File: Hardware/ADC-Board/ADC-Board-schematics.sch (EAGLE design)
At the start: 20 parts

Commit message: layouts
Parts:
- removed CDCS502: CDCS502, components:CDCS502
- removed IC6: (no value), SparkFun-PowerIC:V_REG_TPS76433SOT23-5
- added U$1: CDCS502TSSOP-8, components:CDCS502TSSOP-8
- added U1: (no value), SparkFun-PowerIC:V_REG_LM1117SOT223
- C28: value (none) -> 10uF
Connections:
- net +12VDC: now also U1.IN; no longer IC6.EN, IC6.IN
- net 3V3: now also U$1.VDD; no longer CDCS502.VDD
- net 5VCC: now also U1.OUT, U1.OUT@1; no longer IC6.OUT
- net GND: now also U$1.FS, U$1.GND, U$1.SSC_SEL_0, U$1.SSC_SEL_1, U1.ADJ; no longer CDCS502.FS, CDCS502.GND, CDCS502.SSC_SEL_0, CDCS502.SSC_SEL_1, IC6.GND
- net N$29: now also U$1.XIN; no longer CDCS502.XIN
- net N$30: now also U$1.XOUT; no longer CDCS502.XOUT
- net N$32: now also U$1.CLK_OUT; no longer CDCS502.CLK_OUT
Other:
- moved on the sheet: C28

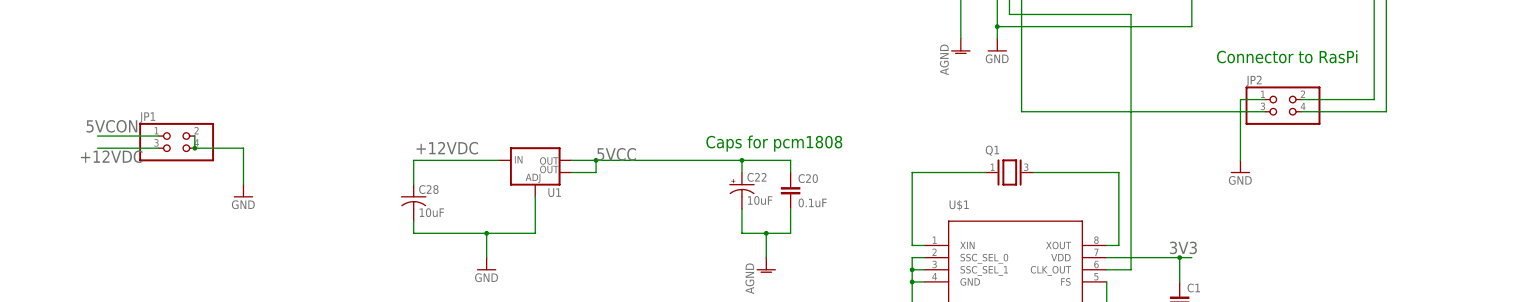
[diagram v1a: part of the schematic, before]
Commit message: tvs considerations
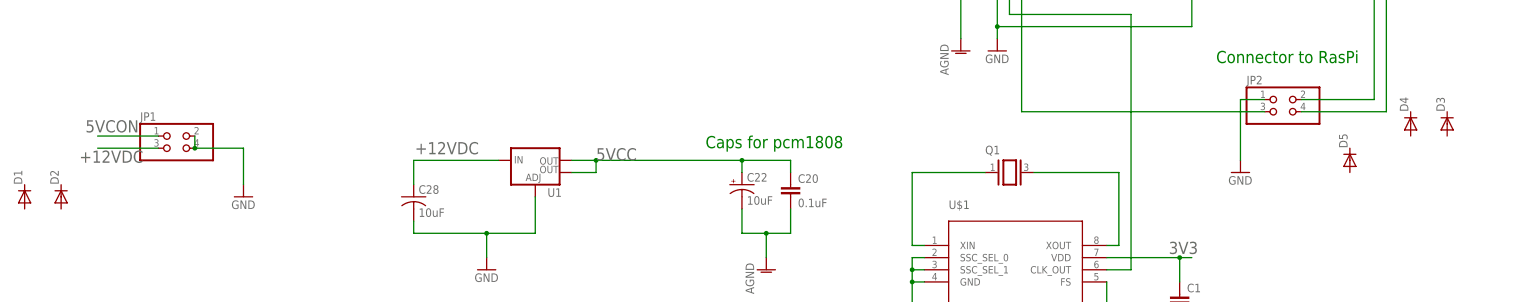
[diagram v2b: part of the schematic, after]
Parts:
- added D1, D2, D3, D4, D5: (no value), diode:DIODE-DO-214AC
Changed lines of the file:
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@@
 <grid distance="0.1" unitdist="inch" unit="inch" style="lines" multiple="1" display="no" altdistance="0.01" altunitdist="inch" altunit="inch"/>
 <layers>
-<layer number="1" name="Top" color="4" fill="1" visible="yes" active="no"/>
-<layer number="2" name="Route2" color="1" fill="3" visible="yes" active="no"/>
-<layer number="3" name="Route3" color="4" fill="3" visible="yes" active="no"/>
-<layer number="4" name="Route4" color="1" fill="4" visible="yes" active="no"/>
-<layer number="5" name="Route5" color="4" fill="4" visible="yes" active="no"/>
-<layer number="6" name="Route6" color="1" fill="8" visible="yes" active="no"/>
-<layer number="7" name="Route7" color="4" fill="8" visible="yes" active="no"/>
-<layer number="8" name="Route8" color="1" fill="2" visible="yes" active="no"/>
-<layer number="9" name="Route9" color="4" fill="2" visible="yes" active="no"/>
-<layer number="10" name="Route10" color="1" fill="7" visible="yes" active="no"/>
-<layer number="11" name="Route11" color="4" fill="7" visible="yes" active="no"/>
-<layer number="12" name="Route12" color="1" fill="5" visible="yes" active="no"/>
-<layer number="13" name="Route13" color="4" fill="5" visible="yes" active="no"/>
-<layer number="14" name="Route14" color="1" fill="6" visible="yes" active="no"/>
-<layer number="15" name="Route15" color="4" fill="6" visible="yes" active="no"/>
-<layer number="16" name="Bottom" color="1" fill="1" visible="yes" active="no"/>
-<layer number="17" name="Pads" color="2" fill="1" visible="yes" active="no"/>
-<layer number="18" name="Vias" color="2" fill="1" visible="yes" active="no"/>
-<layer number="19" name="Unrouted" color="6" fill="1" visible="yes" active="no"/>
-<layer number="20" name="Dimension" color="15" fill="1" visible="yes" active="no"/>
-<layer number="21" name="tPlace" color="7" fill="1" visible="yes" active="no"/>
-<layer number="22" name="bPlace" color="7" fill="1" visible="yes" active="no"/>
-<layer number="23" name="tOrigins" color="15" fill="1" visible="yes" active="no"/>
-<layer number="24" name="bOrigins" color="15" fill="1" visible="yes" active="no"/>
-<layer number="25" name="tNames" color="7" fill="1" visible="yes" active="no"/>
-<layer number="26" name="bNames" color="7" fill="1" visible="yes" active="no"/>
-<layer number="27" name="tValues" color="7" fill="1" visible="yes" active="no"/>
-<layer number="28" name="bValues" color="7" fill="1" visible="yes" active="no"/>
+<layer number="1" name="Top" color="4" fill="1" visible="no" active="no"/>
+<layer number="2" name="Route2" color="1" fill="3" visible="no" active="no"/>
+<layer number="3" name="Route3" color="4" fill="3" visible="no" active="no"/>
+<layer number="4" name="Route4" color="1" fill="4" visible="no" active="no"/>
+<layer number="5" name="Route5" color="4" fill="4" visible="no" active="no"/>
+<layer number="6" name="Route6" color="1" fill="8" visible="no" active="no"/>
+<layer number="7" name="Route7" color="4" fill="8" visible="no" active="no"/>
+<layer number="8" name="Route8" color="1" fill="2" visible="no" active="no"/>
+<layer number="9" name="Route9" color="4" fill="2" visible="no" active="no"/>
+<layer number="10" name="Route10" color="1" fill="7" visible="no" active="no"/>
+<layer number="11" name="Route11" color="4" fill="7" visible="no" active="no"/>
+<layer number="12" name="Route12" color="1" fill="5" visible="no" active="no"/>
+<layer number="13" name="Route13" color="4" fill="5" visible="no" active="no"/>
+<layer number="14" name="Route14" color="1" fill="6" visible="no" active="no"/>
+<layer number="15" name="Route15" color="4" fill="6" visible="no" active="no"/>
+<layer number="16" name="Bottom" color="1" fill="1" visible="no" active="no"/>
+<layer number="17" name="Pads" color="2" fill="1" visible="no" active="no"/>
+<layer number="18" name="Vias" color="2" fill="1" visible="no" active="no"/>
+<layer number="19" name="Unrouted" color="6" fill="1" visible="no" active="no"/>
+<layer number="20" name="Dimension" color="15" fill="1" visible="no" active="no"/>
+<layer number="21" name="tPlace" color="7" fill="1" visible="no" active="no"/>
+<layer number="22" name="bPlace" color="7" fill="1" visible="no" active="no"/>
+<layer number="23" name="tOrigins" color="15" fill="1" visible="no" active="no"/>
+<layer number="24" name="bOrigins" color="15" fill="1" visible="no" active="no"/>
+<layer number="25" name="tNames" color="7" fill="1" visible="no" active="no"/>
+<layer number="26" name="bNames" color="7" fill="1" visible="no" active="no"/>
+<layer number="27" name="tValues" color="7" fill="1" visible="no" active="no"/>
+<layer number="28" name="bValues" color="7" fill="1" visible="no" active="no"/>
 <layer number="29" name="tStop" color="7" fill="3" visible="no" active="no"/>
 <layer number="30" name="bStop" color="7" fill="6" visible="no" active="no"/>
@@
 <layer number="35" name="tGlue" color="7" fill="4" visible="no" active="no"/>
 <layer number="36" name="bGlue" color="7" fill="5" visible="no" active="no"/>
-<layer number="37" name="tTest" color="7" fill="1" visible="yes" active="no"/>
-<layer number="38" name="bTest" color="7" fill="1" visible="yes" active="no"/>
+<layer number="37" name="tTest" color="7" fill="1" visible="no" active="no"/>
+<layer number="38" name="bTest" color="7" fill="1" visible="no" active="no"/>
 <layer number="39" name="tKeepout" color="4" fill="11" visible="no" active="no"/>
 <layer number="40" name="bKeepout" color="1" fill="11" visible="no" active="no"/>
@@
 <layer number="44" name="Drills" color="7" fill="1" visible="no" active="no"/>
 <layer number="45" name="Holes" color="7" fill="1" visible="no" active="no"/>
-<layer number="46" name="Milling" color="3" fill="1" visible="yes" active="no"/>
-<layer number="47" name="Measures" color="7" fill="1" visible="yes" active="no"/>
-<layer number="48" name="Document" color="7" fill="1" visible="yes" active="no"/>
-<layer number="49" name="Reference" color="7" fill="1" visible="yes" active="no"/>
-<layer number="50" name="dxf" color="7" fill="1" visible="yes" active="no"/>
-<layer number="51" name="tDocu" color="7" fill="1" visible="yes" active="no"/>
-<layer number="52" name="bDocu" color="7" fill="1" visible="yes" active="no"/>
-<layer number="53" name="tGND_GNDA" color="7" fill="9" visible="yes" active="no"/>
-<layer number="54" name="bGND_GNDA" color="1" fill="9" visible="yes" active="no"/>
-<layer number="56" name="wert" color="7" fill="1" visible="yes" active="no"/>
-<layer number="57" name="tCAD" color="7" fill="1" visible="yes" active="no"/>
-<layer number="59" name="tCarbon" color="7" fill="1" visible="yes" active="no"/>
-<layer number="60" name="bCarbon" color="7" fill="1" visible="yes" active="no"/>
+<layer number="46" name="Milling" color="3" fill="1" visible="no" active="no"/>
+<layer number="47" name="Measures" color="7" fill="1" visible="no" active="no"/>
+<layer number="48" name="Document" color="7" fill="1" visible="no" active="no"/>
+<layer number="49" name="Reference" color="7" fill="1" visible="no" active="no"/>
+<layer number="50" name="dxf" color="7" fill="1" visible="no" active="no"/>
+<layer number="51" name="tDocu" color="7" fill="1" visible="no" active="no"/>
+<layer number="52" name="bDocu" color="7" fill="1" visible="no" active="no"/>
+<layer number="53" name="tGND_GNDA" color="7" fill="9" visible="no" active="no"/>
+<layer number="54" name="bGND_GNDA" color="1" fill="9" visible="no" active="no"/>
+<layer number="56" name="wert" color="7" fill="1" visible="no" active="no"/>
+<layer number="57" name="tCAD" color="7" fill="1" visible="no" active="no"/>
+<layer number="59" name="tCarbon" color="7" fill="1" visible="no" active="no"/>
+<layer number="60" name="bCarbon" color="7" fill="1" visible="no" active="no"/>
 <layer number="90" name="Modules" color="5" fill="1" visible="yes" active="yes"/>
 <layer number="91" name="Nets" color="2" fill="1" visible="yes" active="yes"/>
@@
 <part name="U1" library="SparkFun-PowerIC" deviceset="V_REG_LM1117" device="SOT223"/>
 <part name="U$1" library="components" deviceset="CDCS502" device="TSSOP-8"/>
+<part name="D1" library="diode" deviceset="DIODE-" device="DO-214AC"/>
+<part name="D2" library="diode" deviceset="DIODE-" device="DO-214AC"/>
+<part name="D3" library="diode" deviceset="DIODE-" device="DO-214AC"/>
+<part name="D4" library="diode" deviceset="DIODE-" device="DO-214AC"/>
+<part name="D5" library="diode" deviceset="DIODE-" device="DO-214AC"/>
 </parts>
 <sheets>
@@
 <instance part="U1" gate="G$1" x="-2.54" y="-5.08"/>
 <instance part="U$1" gate="G$1" x="93.98" y="-27.94"/>
+<instance part="D1" gate="G$1" x="-109.22" y="-12.7" rot="R90"/>
+<instance part="D2" gate="G$1" x="-101.6" y="-12.7" rot="R90"/>
+<instance part="D3" gate="G$1" x="187.96" y="2.54" rot="R90"/>
+<instance part="D4" gate="G$1" x="180.34" y="2.54" rot="R90"/>
+<instance part="D5" gate="G$1" x="167.64" y="-5.08" rot="R90"/>
 </instances>
 <busses>

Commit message: adc-board
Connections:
- net 5VCC: now also C27.1, TLV71333.EN, TLV71333.IN
- net 5VCON: no longer C27.1, TLV71333.EN, TLV71333.IN
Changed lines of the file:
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@@
 <net name="5VCON" class="0">
-<segment>
-<wire x1="-55.88" y1="58.42" x2="-63.5" y2="58.42" width="0.1524" layer="91"/>
-<label x="-78.74" y="58.42" size="2.54" layer="95"/>
-<pinref part="C27" gate="G$1" pin="1"/>
-<wire x1="-63.5" y1="58.42" x2="-76.2" y2="58.42" width="0.1524" layer="91"/>
-<wire x1="-76.2" y1="58.42" x2="-78.74" y2="58.42" width="0.1524" layer="91"/>
-<wire x1="-76.2" y1="58.42" x2="-76.2" y2="55.88" width="0.1524" layer="91"/>
-<junction x="-76.2" y="58.42"/>
-<wire x1="-55.88" y1="48.26" x2="-63.5" y2="48.26" width="0.1524" layer="91"/>
-<wire x1="-63.5" y1="48.26" x2="-63.5" y2="58.42" width="0.1524" layer="91"/>
-<junction x="-63.5" y="58.42"/>
-<pinref part="TLV71333" gate="G$1" pin="IN"/>
-<pinref part="TLV71333" gate="G$1" pin="EN"/>
-</segment>
 <segment>
 <pinref part="JP1" gate="A" pin="1"/>
@@
 <pinref part="PCM1808" gate="G$1" pin="VCC"/>
 </segment>
-</net>
+<segment>
+<wire x1="-55.88" y1="58.42" x2="-63.5" y2="58.42" width="0.1524" layer="91"/>
+<label x="-78.74" y="58.42" size="2.54" layer="95"/>
+<pinref part="C27" gate="G$1" pin="1"/>
+<wire x1="-63.5" y1="58.42" x2="-76.2" y2="58.42" width="0.1524" layer="91"/>
+<wire x1="-76.2" y1="58.42" x2="-78.74" y2="58.42" width="0.1524" layer="91"/>
+<wire x1="-76.2" y1="58.42" x2="-76.2" y2="55.88" width="0.1524" layer="91"/>
+<junction x="-76.2" y="58.42"/>
+<wire x1="-55.88" y1="48.26" x2="-63.5" y2="48.26" width="0.1524" layer="91"/>
+<wire x1="-63.5" y1="48.26" x2="-63.5" y2="58.42" width="0.1524" layer="91"/>
+<junction x="-63.5" y="58.42"/>
+<pinref part="TLV71333" gate="G$1" pin="IN"/>
+<pinref part="TLV71333" gate="G$1" pin="EN"/>
+</segment>
+</net>

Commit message: HW
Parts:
- added U$2, U$3: 3MM5-PLUG, Pekkas_libraries:3MM5-PLUG
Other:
- moved on the sheet: JP4
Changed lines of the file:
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@@
 <part name="D4" library="diode" deviceset="DIODE-" device="DO-214AC"/>
 <part name="D5" library="diode" deviceset="DIODE-" device="DO-214AC"/>
+<part name="U$2" library="Pekkas_libraries" deviceset="3MM5-PLUG" device=""/>
+<part name="U$3" library="Pekkas_libraries" deviceset="3MM5-PLUG" device=""/>
 </parts>
 <sheets>
@@
 <instance part="GND" gate="1" x="76.2" y="-53.34"/>
 <instance part="GND19" gate="1" x="144.78" y="-7.62"/>
-<instance part="JP4" gate="A" x="195.58" y="45.72"/>
-<instance part="AGND3" gate="VR1" x="205.74" y="38.1"/>
+<instance part="JP4" gate="A" x="231.14" y="45.72"/>
+<instance part="AGND3" gate="VR1" x="254" y="38.1"/>
 <instance part="PCM1808" gate="G$1" x="114.3" y="40.64"/>
 <instance part="JP1" gate="A" x="-76.2" y="-2.54"/>
@@
 <instance part="D4" gate="G$1" x="180.34" y="2.54" rot="R90"/>
 <instance part="D5" gate="G$1" x="167.64" y="-5.08" rot="R90"/>
+<instance part="U$2" gate="G$1" x="223.52" y="20.32"/>
+<instance part="U$3" gate="G$1" x="223.52" y="2.54"/>
 </instances>
 <busses>
@@
 <pinref part="JP4" gate="A" pin="2"/>
 <pinref part="AGND3" gate="VR1" pin="AGND"/>
-<wire x1="198.12" y1="48.26" x2="205.74" y2="48.26" width="0.1524" layer="91"/>
-<wire x1="205.74" y1="48.26" x2="205.74" y2="40.64" width="0.1524" layer="91"/>
+<wire x1="233.68" y1="48.26" x2="254" y2="48.26" width="0.1524" layer="91"/>
+<wire x1="254" y1="48.26" x2="254" y2="40.64" width="0.1524" layer="91"/>
 </segment>
 </net>
@@
 <segment>
 <pinref part="C24" gate="G$1" pin="-"/>
-<wire x1="157.48" y1="48.26" x2="190.5" y2="48.26" width="0.1524" layer="91"/>
+<wire x1="157.48" y1="48.26" x2="226.06" y2="48.26" width="0.1524" layer="91"/>
 <pinref part="JP4" gate="A" pin="1"/>
 </segment>
@@
 <pinref part="C25" gate="G$1" pin="-"/>
 <pinref part="JP4" gate="A" pin="3"/>
-<wire x1="167.64" y1="45.72" x2="190.5" y2="45.72" width="0.1524" layer="91"/>
-</segment>
-</net>
+<wire x1="167.64" y1="45.72" x2="226.06" y2="45.72" width="0.1524" layer="91"/>
+</segment>
+</net>

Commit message: some hw changes
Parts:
- removed U$2, U$3: 3MM5-PLUG, Pekkas_libraries:3MM5-PLUG
- added C2, C3: 82pF, SparkFun-Passives:CAP0603-CAP
- added C4, VAR1, VAR2: (no value), SparkFun-Passives:CAP0603-CAP
- added IN-L, IN-R: 3MM5-PLUG, Pekkas_libraries:3MM5-PLUG
- added R10, R5: 20, SparkFun-Passives:RESISTOR0603-RES
- added R2, R7: (no value), SparkFun-Passives:RESISTOR0603-RES
- added R3, R4, R8, R9: 4k7, SparkFun-Passives:RESISTOR0603-RES
- added U2: OPA2348AIDCNTG4, Pekkas_libraries:OPA2348AIDCNTG4
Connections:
- removed net N$28: C25.+, PCM1808.VINL
- removed net N$36: C24.-, JP4.1
- removed net N$37: C25.-, JP4.3
- new net AGND: C2.2, C3.2, C4.2, IN-L.GND, IN-R.GND, R2.1, R3.1, R7.2, R9.2, U2.V-, VAR1.2, VAR2.2
- new net N$10: R10.2, U2.-IN_B, U2.OUT_B
- new net N$11: C2.1, PCM1808.VINR, R10.1
- new net N$12: IN-R.+, JP4.1
- new net N$13: IN-L.+, JP4.3
- new net N$5: C24.+, R3.2, R4.1, U2.+IN_B, VAR2.1
- new net N$6: R5.1, U2.-IN_A, U2.OUT_A
- new net N$7: C3.1, PCM1808.VINL, R5.2
- new net N$8: C25.-, R7.1
- new net N$9: C25.+, R8.2, R9.1, U2.+IN_A, VAR1.1
- net 5VCC: now also C4.1, R4.2, R8.1, U2.V+
- net N$3: now also C24.-, R2.2; no longer C24.+, PCM1808.VINR
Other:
- note added: "potikka ks exel"
- note removed: "Muuta tämä kahdeksi 3.5mm mono socketiksi"
- moved on the sheet: C24, C25, D3, D4, D5, JP2, JP4

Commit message: HW
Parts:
- removed D1, D2, D3, D4, D5: (no value), diode:DIODE-DO-214AC
- added POT1, POT2: TRIMPOT-PVZ2A, SparkFun-Resistors:TRIMPOT-PVZ2A
- added VAR3, VAR4, VAR5: (no value), SparkFun-Passives:CAP0603-CAP
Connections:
- removed net N$12: IN-R.+, JP4.1
- removed net N$13: IN-L.+, JP4.3
- new net N$20: IN-L.+, JP4.3, POT2.S
- new net N$21: IN-R.+, JP4.1, POT1.S
- net GND: now also VAR3.2, VAR4.2, VAR5.2
- net N$1: now also VAR4.1
- net N$2: now also VAR5.1
- net N$3: now also POT1.E
- net N$4: now also VAR3.1
- net N$8: now also POT2.E
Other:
- note removed: "potikka ks exel"
- moved on the sheet: C1, C2, C20, C21, C22, C23, C24, C25, C26, C27, C28, C29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
